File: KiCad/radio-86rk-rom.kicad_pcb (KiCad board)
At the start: 2 copper layers, 50.8 x 30.5 mm, 9 parts, among them J1 Parallel, U1 27C256

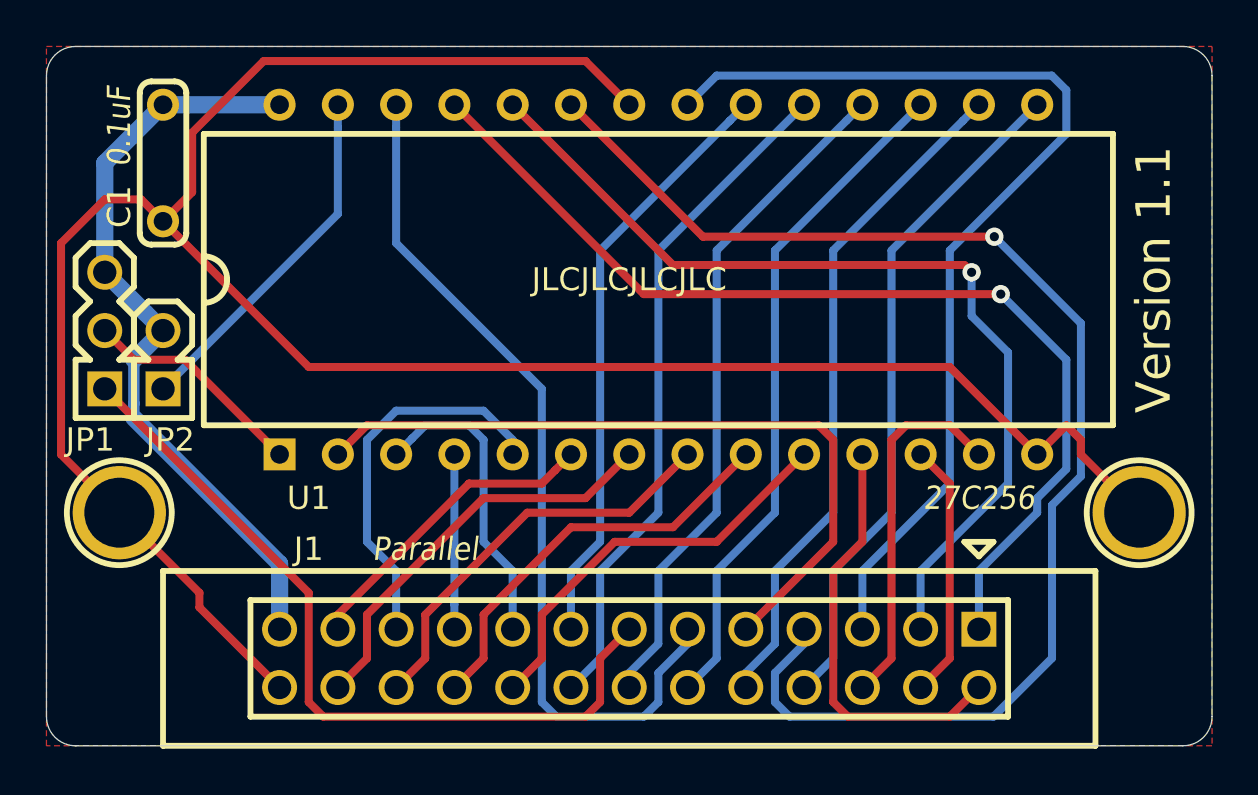
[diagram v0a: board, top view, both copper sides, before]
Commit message: Modernize KiCad project and bundle portable CAD dependencies
Migrate to KiCad 10.0.7 with local symbol, footprint and 3D model libraries. Add populated STEP and FreeCAD exports, validation evidence, and documented remaining ERC/DRC findings while preserving original connectivity and routing.
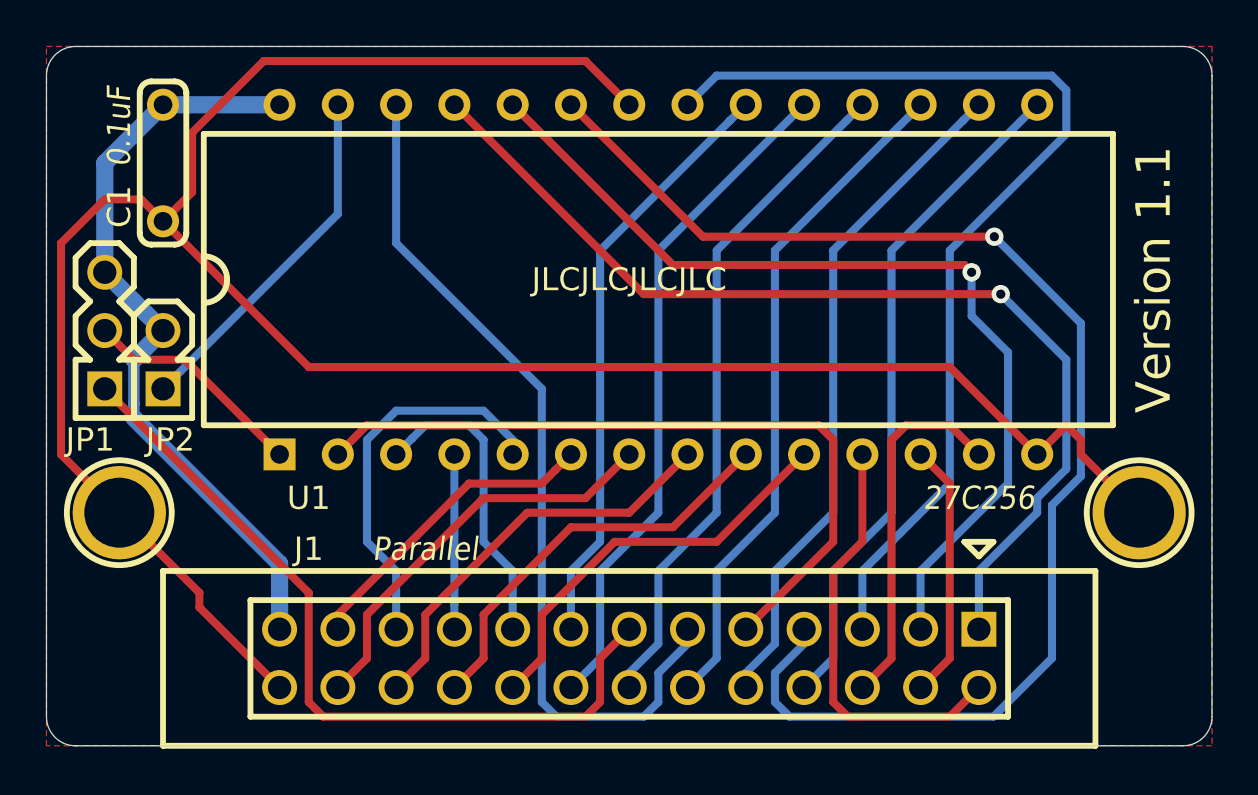
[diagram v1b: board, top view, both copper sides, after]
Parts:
- C1: footprint My_Components:Cap_Cer_508 -> radio-86rk-rom-footprints:Cap_Cer_508
- HOLE1, HOLE2: footprint My_Components:Hole_3mm -> radio-86rk-rom-footprints:Hole_3mm
- J1: footprint My_Components:Conn_Pin_Header_13x2_2.54mm_Shrouded -> radio-86rk-rom-footprints:Conn_Pin_Header_13x2_2.54mm_Shrouded
- JP1: footprint My_Components:Conn_Pin_Header_3x1_2.54mm -> radio-86rk-rom-footprints:Conn_Pin_Header_3x1_2.54mm
- JP2: footprint My_Components:Conn_Pin_Header_2x1_2.54mm -> radio-86rk-rom-footprints:Conn_Pin_Header_2x1_2.54mm
- REF**: footprint Symbol:KiCad-Logo2_5mm_SilkScreen -> radio-86rk-rom-footprints:KiCad-Logo2_5mm_SilkScreen
- REF**: footprint Symbol:OSHW-Logo_5.7x6mm_SilkScreen -> radio-86rk-rom-footprints:OSHW-Logo_5.7x6mm_SilkScreen
- U1: footprint My_Components:IC_DIP28_600 -> radio-86rk-rom-footprints:IC_DIP28_600
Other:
- net class Default removed
- net class Power removed
